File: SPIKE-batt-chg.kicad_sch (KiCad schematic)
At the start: 13 parts, among them IC2 CH224K, J1 USB_C_Receptacle_USB2.0, J3 Barrel_Jack_Switch, Q1 PMOS

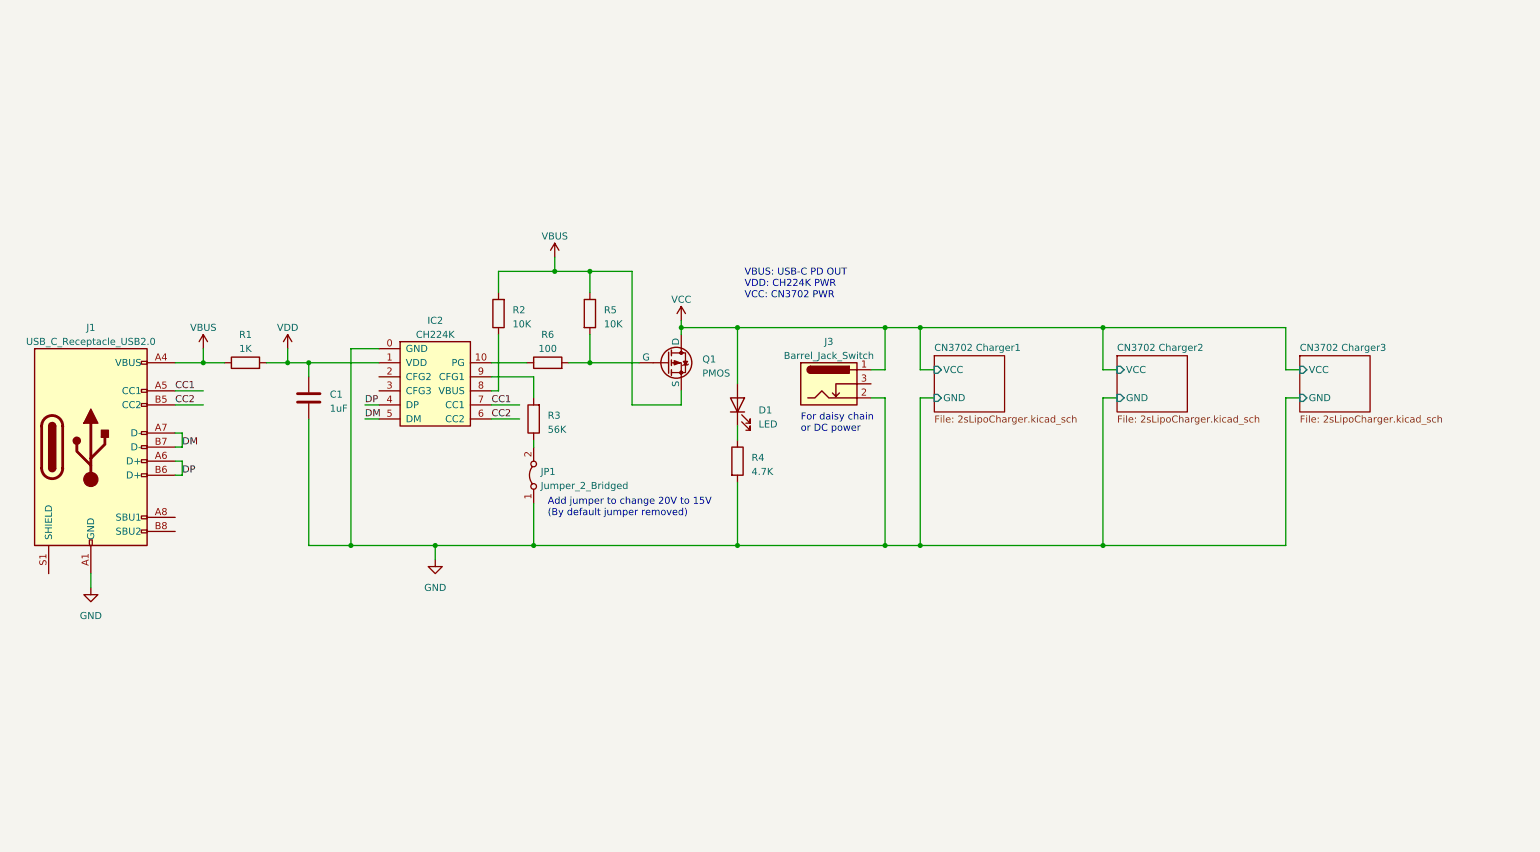
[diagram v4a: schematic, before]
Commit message: Finished footprint assignments, added testpoints
- Added polyfuse
- Cleaned up schematic (mirrored some components for clarity)
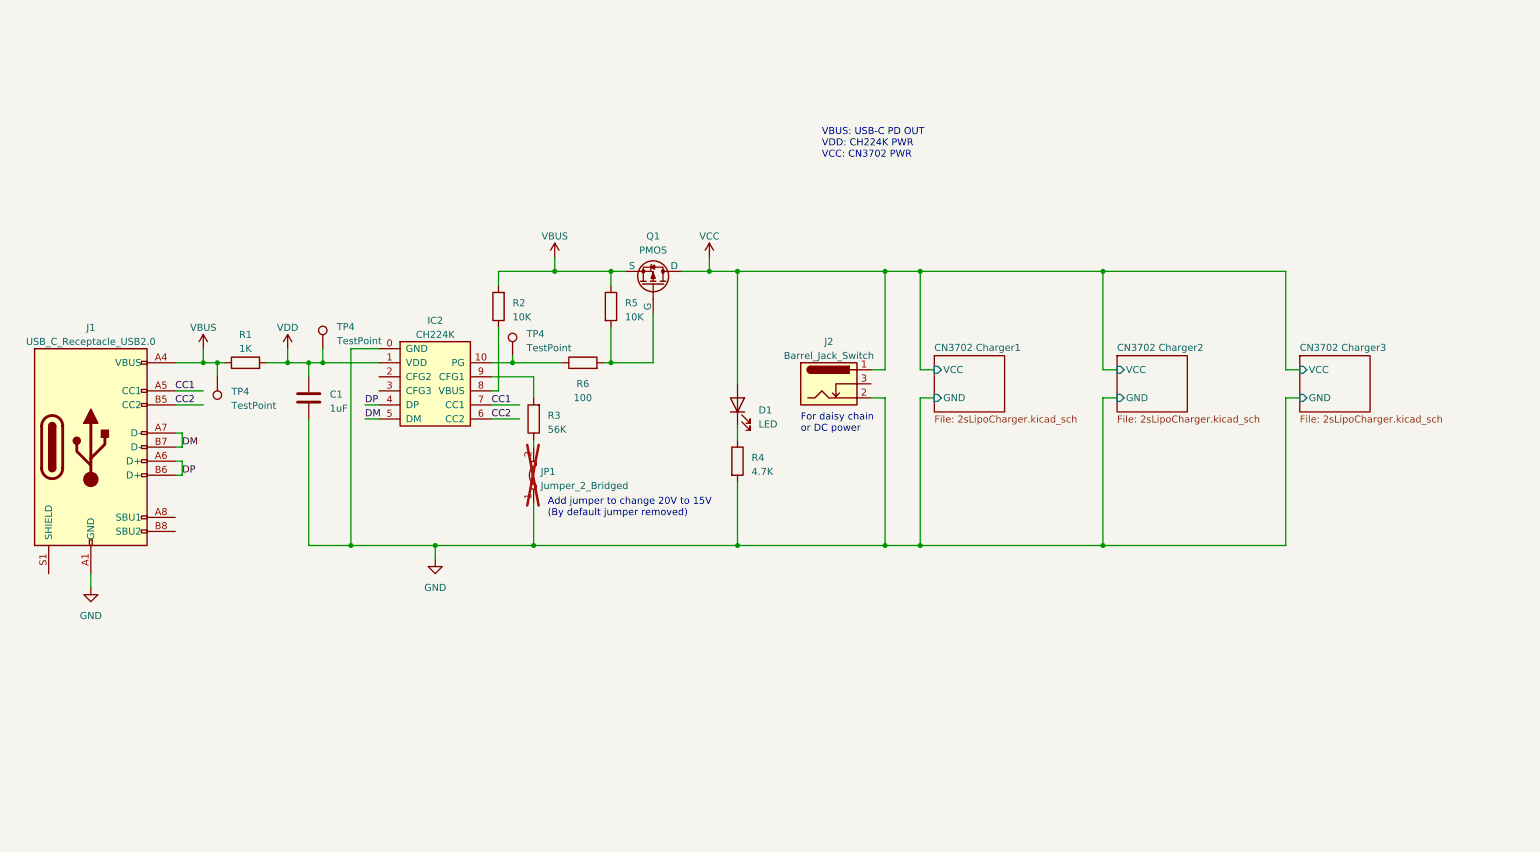
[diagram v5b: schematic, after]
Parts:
- added TP4 (x3): TestPoint, TestPoint:TestPoint_Pad_D2.0mm, symbol Connector:TestPoint
- IC2: footprint (none) -> JH:ESSOP-10_3.9x4.9mm_P1.00mm_EP2.3x3.2mm_ThermalVias
- J1: footprint (none) -> Connector_USB:USB_C_Receptacle_XKB_U262-16XN-4BVC11; JLCPCB Part # (none) -> C2765186; Part (none) -> TYPE-C 16PIN 2MD(073)
- J2: renamed from J3; footprint (none) -> JH:BarrelJack_Lock
- JP1: now not fitted; now left out of the parts list
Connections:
- net VBUS: now also TP4.1
- net VDD: now also TP4.1
- net at IC2.10 (PG), R6.1: now also TP4.1
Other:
- moved on the sheet: Q1, R2, R5, R6

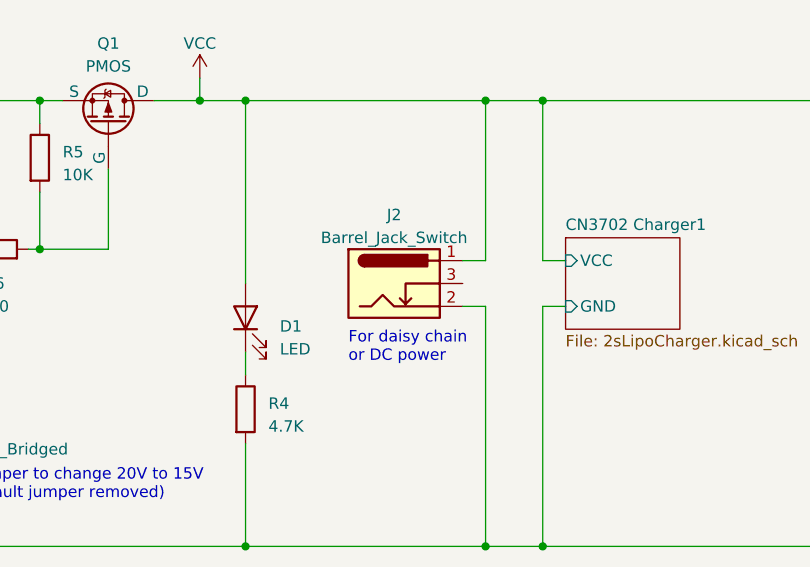
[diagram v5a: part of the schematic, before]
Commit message: Edited DRC, started layout
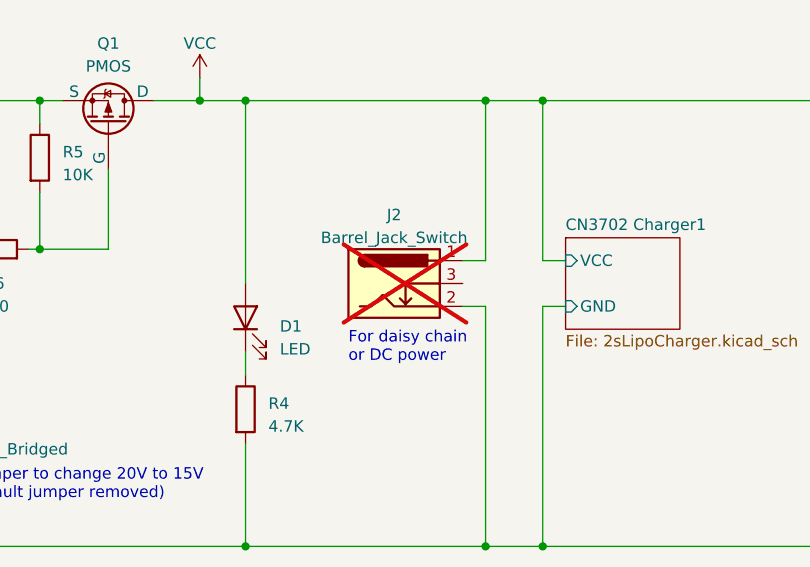
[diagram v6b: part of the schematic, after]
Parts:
- J2: now not fitted; now left out of the parts list
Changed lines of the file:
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@@
   )
   (symbol (lib_id "Connector:Barrel_Jack_Switch") (at 163.83 85.09 0) (unit 1)
-    (in_bom yes) (on_board yes) (dnp no) (fields_autoplaced)
+    (in_bom no) (on_board yes) (dnp yes) (fields_autoplaced)
     (property "Reference" "J2" (at 163.83 77.47 0)
       (effects (font (size 1.27 1.27)))

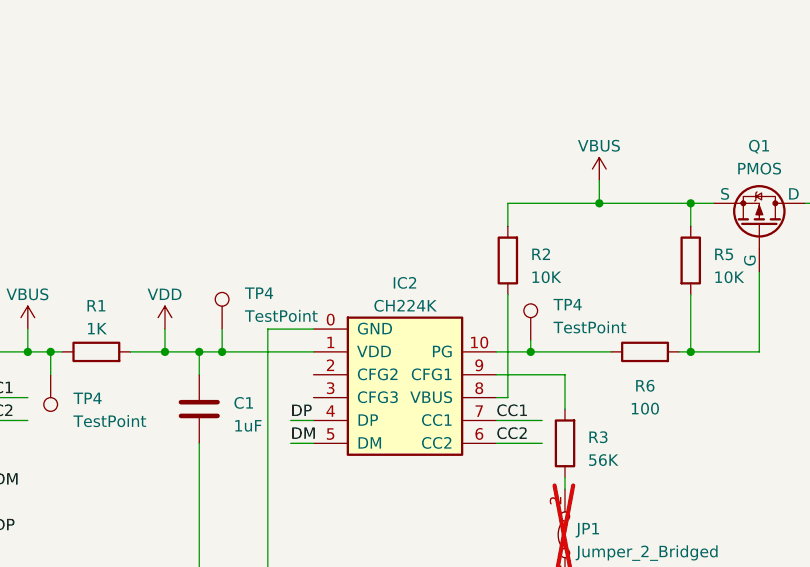
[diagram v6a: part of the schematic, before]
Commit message: CH224K Board Layout complete
- Partial layout of CN3702
- Fixed the incorrect NetTie on 2sLipoCharger.kicad_sch (More things are supposed to go to AGND)
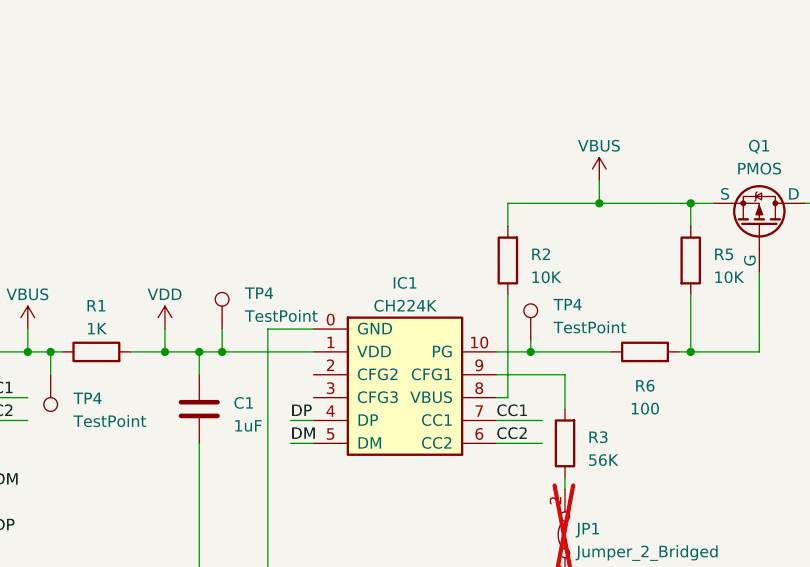
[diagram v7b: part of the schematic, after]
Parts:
- TP4: footprint TestPoint:TestPoint_Pad_D2.0mm -> TestPoint:TestPoint_Pad_D1.0mm
- renumbered IC2 to IC1
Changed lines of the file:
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@@
       (effects (font (size 1.27 1.27)) (justify left))
     )
-    (property "Footprint" "TestPoint:TestPoint_Pad_D2.0mm" (at 111.76 80.01 0)
+    (property "Footprint" "TestPoint:TestPoint_Pad_D1.0mm" (at 111.76 80.01 0)
       (effects (font (size 1.27 1.27)) hide)
     )
@@
       (effects (font (size 1.27 1.27)) (justify left))
     )
-    (property "Footprint" "TestPoint:TestPoint_Pad_D2.0mm" (at 77.47 78.74 0)
+    (property "Footprint" "TestPoint:TestPoint_Pad_D1.0mm" (at 77.47 78.74 0)
       (effects (font (size 1.27 1.27)) hide)
     )
@@
   (symbol (lib_id "Connector_Generic:Conn_02x05_Counter_Clockwise") (at 92.71 86.36 0) (unit 1)
     (in_bom yes) (on_board yes) (dnp no) (fields_autoplaced)
-    (property "Reference" "IC2" (at 92.71 73.66 0)
+    (property "Reference" "IC1" (at 92.71 73.66 0)
       (effects (font (size 1.27 1.27)))
     )
@@
       (project "SPIKE-batt-chg"
         (path "/40189395-1355-465c-9381-a270b42186bd"
-          (reference "IC2") (unit 1)
+          (reference "IC1") (unit 1)
         )
       )
@@
       (effects (font (size 1.27 1.27)) (justify right))
     )
-    (property "Footprint" "TestPoint:TestPoint_Pad_D2.0mm" (at 48.26 83.82 0)
-      (effects (font (size 1.27 1.27)) hide)
-    )
+    (property "Footprint" "TestPoint:TestPoint_Pad_D1.0mm" (at 48.26 83.82 0)
+      (effects (font (size 1.27 1.27)) hide)
+    )

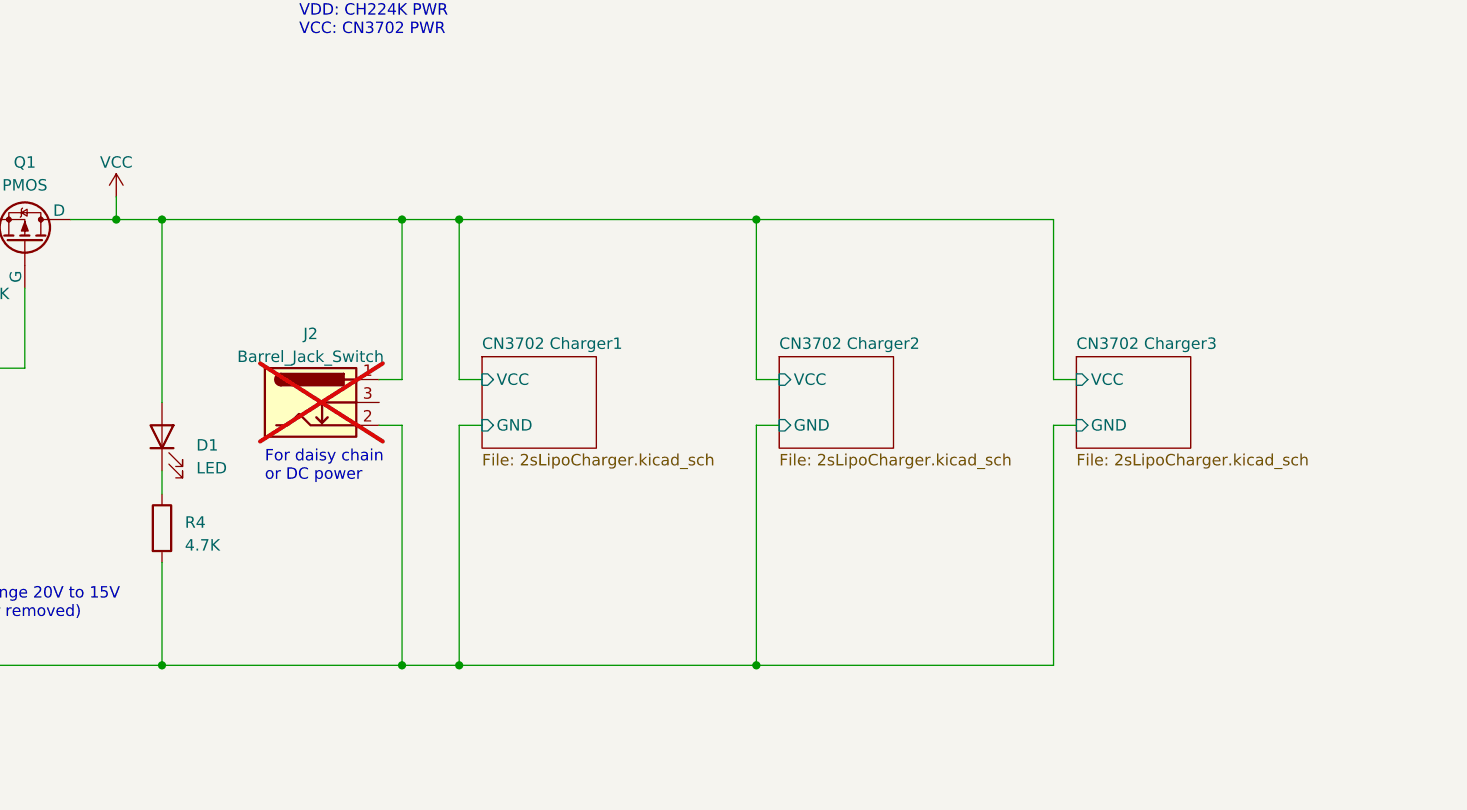
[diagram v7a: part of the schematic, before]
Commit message: Added fuse and shunt diode
For reverse polarity protection
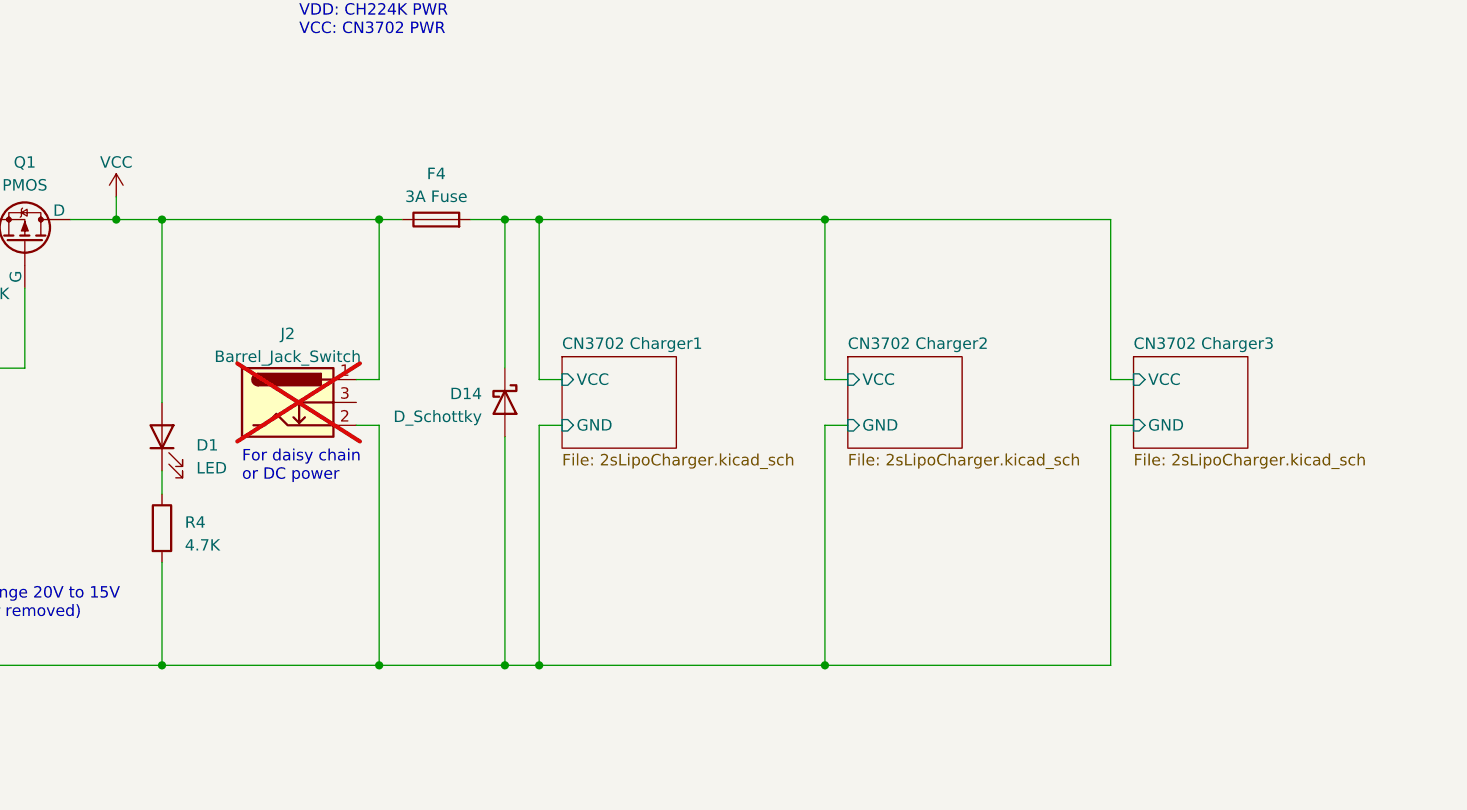
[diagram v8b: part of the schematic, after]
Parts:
- added D14: D_Schottky, Diode_SMD:D_SMA, symbol Device:D_Schottky
- added F4: 3A Fuse, Fuse:Fuse_0603_1608Metric, symbol Device:Fuse
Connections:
- net GND: now also D14.2 (A)
- net VCC: now also F4.1
- new net CN3702 Charger1/VCC: D14.1 (K), F4.2
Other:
- moved on the sheet: J2
